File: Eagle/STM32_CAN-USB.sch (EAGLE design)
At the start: 42 parts, among them IC1 STM32F105RBT, IC2 TJA1055T, IC4 LM1117IMPX-3.3, Q1 16MHz, X1 MINI-USB

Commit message: Revert sch & brd
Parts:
- removed MC34063: MC34063, STM32_CAN-USB:MC34063
- removed R11: 3K, rcl:R-EU_R0805
- added C15: 10uF, rcl:CPOL-US153CLV-0605
- added C19, C22: 1nF, rcl:C-EUC0805
- added C20, C23: 0.1, rcl:C-EUC0805
- added C21, C24: 4.7uF, rcl:C-EUC0805
- added D1: SS26, STM32_CAN-USB:SCHOTTKY-DIODESMD
- added D2: SK36A, STM32_CAN-USB:SK36A
- added DR2: CDRH3D16NP 6.8uH, STM32_CAN-USB:CDRH3D16NP
- added F1: EST-157000 2A, STM32_CAN-USB:FUSE
- added IC3: BD9G101G, STM32_CAN-USB:BD9G101G
- C11: value 10uF/16v -> 100uF/16v; device rcl:CPOL-EUSMCA -> rcl:CPOL-US153CLV-0605
- C12: value 220uF/35V -> 0.015uF; device rcl:CPOL-EU153CLV-0810 -> rcl:C-EUC0805
- C13: value 220pF -> 0.1
- C14: value 220uF/35V -> 4.7uF/50v; device rcl:CPOL-EU153CLV-0810 -> rcl:CPOL-US153CLV-0605
- C16: value 220uF/16 -> 10uF
- D3: value SS14 -> SM6T18CA; device STM32_CAN-USB:SS14 -> STM32_CAN-USB:SM6T18CA
- DR1: value 220uH -> CDRH127 100u
- R7: value 0.33 -> 680
- R8: value 1K -> 3.9K
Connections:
- net TJA_EN renamed N$14
- net TJA_ERR renamed N$15
- net TJA_RXD renamed N$4
- net TJA_STB renamed N$6
- net TJA_TXD renamed N$5
- new net N$17: C22.1, C23.1, C24.1, D2.A, D3.2, DR1.2
- net +12V: now also F1.1; no longer C12.+, MC34063.VIN, R7.1
- net +5V: now also C13.2, C15.+, DR2.2, R8.1; no longer C14.+, DR1.1, R11.1
- net BAT: now also C14.+, D2.C, IC3.VCC
- net EN: now also IC3.EN
- net GND: now also C15.-, C19.2, C20.2, C21.2, C22.2, C23.2, C24.2, D1.A, D3.1, IC3.GND, R7.1; no longer C12.-, C13.2, D3.A, MC34063.GND, R8.2
- net N$12: now also C12.2, D1.C, DR2.1, IC3.LX; no longer MC34063.CMPR, R11.2, R8.1
- net N$13: now also C13.1, IC3.FB, R7.2, R8.2; no longer D3.C, DR1.2, MC34063.SWE
- net N$18: now also C19.1, C20.1, C21.1, DR1.1, F1.2; no longer C13.1, MC34063.CT
- net N$9: now also C12.1, IC3.BST; no longer MC34063.DRVC, MC34063.IPK, MC34063.SWC, R7.2
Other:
- moved on the sheet: C11, C13, C14, C16, C17, C18, DR1, IC4, JP1, R7, R8

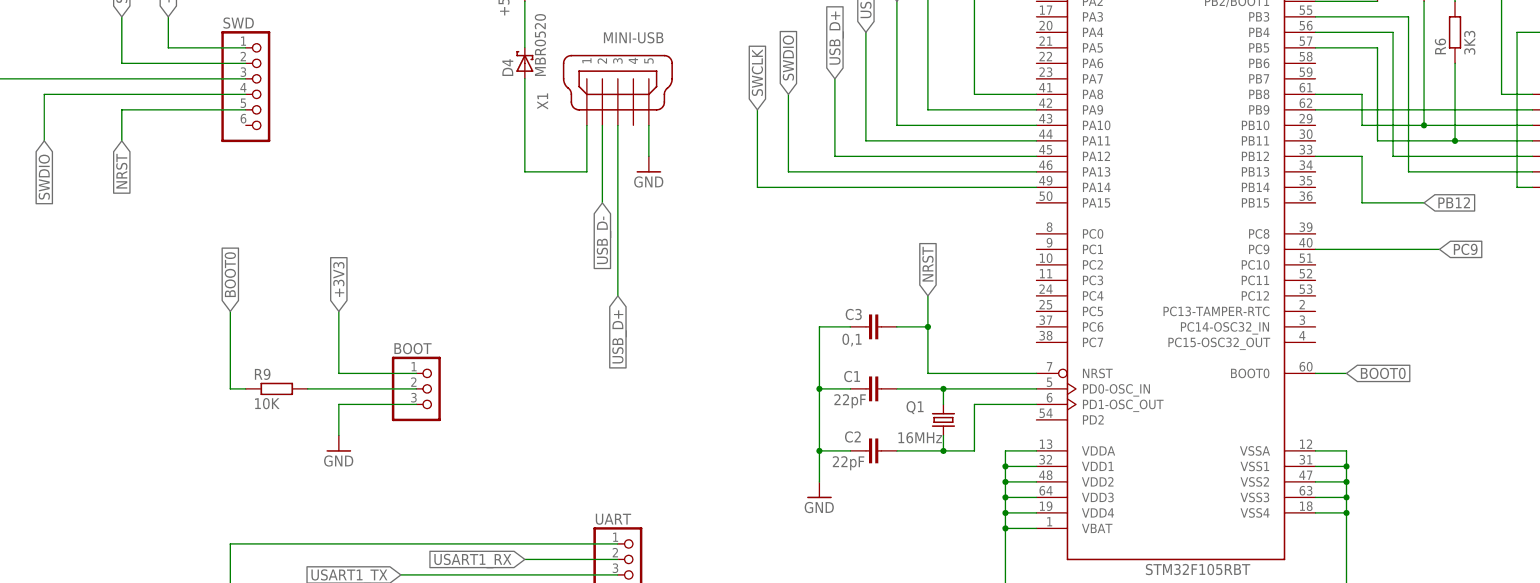
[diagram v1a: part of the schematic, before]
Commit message: delete boot, edit SWD
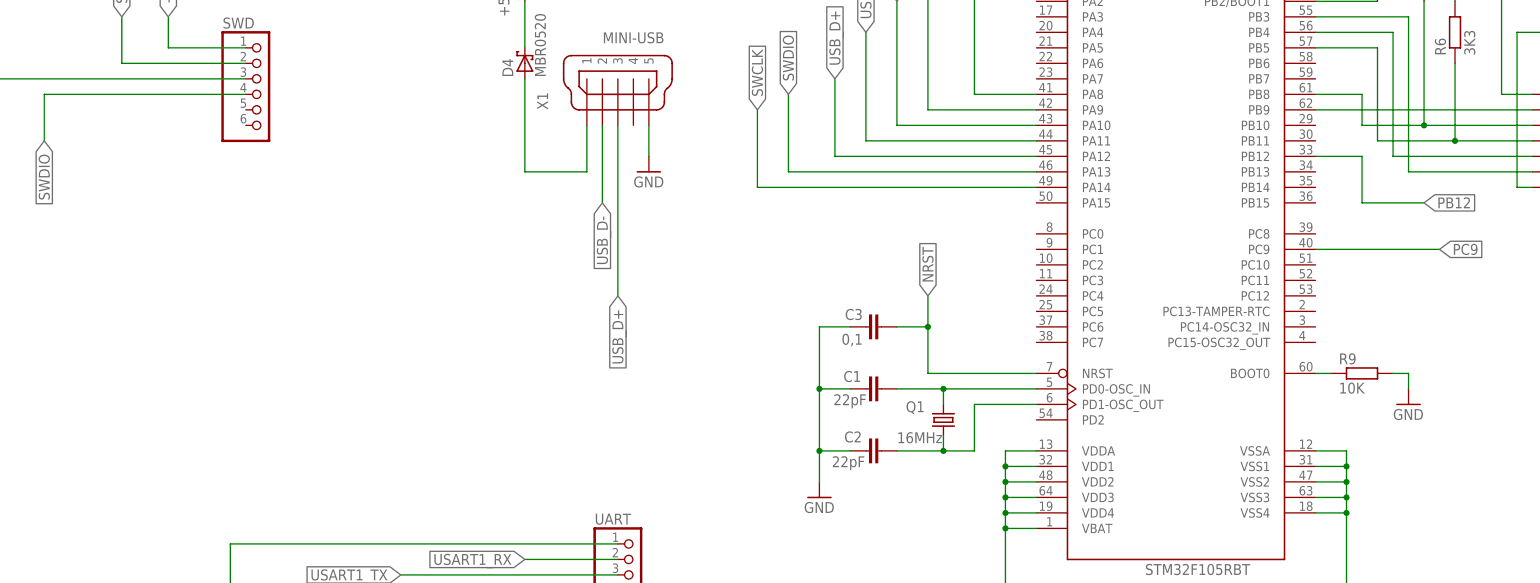
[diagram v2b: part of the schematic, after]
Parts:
- removed BOOT: (no value), pinhead:PINHD-1X3
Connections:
- net BOOT0 renamed N$3
- removed net N$3 (its old number): BOOT.2, R9.2
- net +3V3: no longer BOOT.1
- net GND: now also R9.2; no longer BOOT.3
- net NRST: no longer SWD.5
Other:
- moved on the sheet: R9
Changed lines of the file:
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@@
 <grid distance="0.1" unitdist="inch" unit="inch" style="lines" multiple="1" display="no" altdistance="0.01" altunitdist="inch" altunit="inch"/>
 <layers>
-<layer number="1" name="Top" color="4" fill="1" visible="no" active="no"/>
-<layer number="16" name="Bottom" color="1" fill="1" visible="no" active="no"/>
-<layer number="17" name="Pads" color="2" fill="1" visible="no" active="no"/>
-<layer number="18" name="Vias" color="2" fill="1" visible="no" active="no"/>
-<layer number="19" name="Unrouted" color="6" fill="1" visible="no" active="no"/>
-<layer number="20" name="Dimension" color="15" fill="1" visible="no" active="no"/>
-<layer number="21" name="tPlace" color="7" fill="1" visible="no" active="no"/>
-<layer number="22" name="bPlace" color="7" fill="1" visible="no" active="no"/>
-<layer number="23" name="tOrigins" color="15" fill="1" visible="no" active="no"/>
-<layer number="24" name="bOrigins" color="15" fill="1" visible="no" active="no"/>
-<layer number="25" name="tNames" color="7" fill="1" visible="no" active="no"/>
-<layer number="26" name="bNames" color="7" fill="1" visible="no" active="no"/>
-<layer number="27" name="tValues" color="7" fill="1" visible="no" active="no"/>
-<layer number="28" name="bValues" color="7" fill="1" visible="no" active="no"/>
+<layer number="1" name="Top" color="4" fill="1" visible="yes" active="no"/>
+<layer number="16" name="Bottom" color="1" fill="1" visible="yes" active="no"/>
+<layer number="17" name="Pads" color="2" fill="1" visible="yes" active="no"/>
+<layer number="18" name="Vias" color="2" fill="1" visible="yes" active="no"/>
+<layer number="19" name="Unrouted" color="6" fill="1" visible="yes" active="no"/>
+<layer number="20" name="Dimension" color="15" fill="1" visible="yes" active="no"/>
+<layer number="21" name="tPlace" color="7" fill="1" visible="yes" active="no"/>
+<layer number="22" name="bPlace" color="7" fill="1" visible="yes" active="no"/>
+<layer number="23" name="tOrigins" color="15" fill="1" visible="yes" active="no"/>
+<layer number="24" name="bOrigins" color="15" fill="1" visible="yes" active="no"/>
+<layer number="25" name="tNames" color="7" fill="1" visible="yes" active="no"/>
+<layer number="26" name="bNames" color="7" fill="1" visible="yes" active="no"/>
+<layer number="27" name="tValues" color="7" fill="1" visible="yes" active="no"/>
+<layer number="28" name="bValues" color="7" fill="1" visible="yes" active="no"/>
 <layer number="29" name="tStop" color="7" fill="3" visible="no" active="no"/>
 <layer number="30" name="bStop" color="7" fill="6" visible="no" active="no"/>
@@
 <layer number="35" name="tGlue" color="7" fill="4" visible="no" active="no"/>
 <layer number="36" name="bGlue" color="7" fill="5" visible="no" active="no"/>
-<layer number="37" name="tTest" color="7" fill="1" visible="no" active="no"/>
-<layer number="38" name="bTest" color="7" fill="1" visible="no" active="no"/>
+<layer number="37" name="tTest" color="7" fill="1" visible="yes" active="no"/>
+<layer number="38" name="bTest" color="7" fill="1" visible="yes" active="no"/>
 <layer number="39" name="tKeepout" color="4" fill="11" visible="no" active="no"/>
 <layer number="40" name="bKeepout" color="1" fill="11" visible="no" active="no"/>
@@
 <layer number="44" name="Drills" color="7" fill="1" visible="no" active="no"/>
 <layer number="45" name="Holes" color="7" fill="1" visible="no" active="no"/>
-<layer number="46" name="Milling" color="3" fill="1" visible="no" active="no"/>
-<layer number="47" name="Measures" color="7" fill="1" visible="no" active="no"/>
-<layer number="48" name="Document" color="7" fill="1" visible="no" active="no"/>
-<layer number="49" name="Reference" color="7" fill="1" visible="no" active="no"/>
-<layer number="51" name="tDocu" color="7" fill="1" visible="no" active="no"/>
-<layer number="52" name="bDocu" color="7" fill="1" visible="no" active="no"/>
+<layer number="46" name="Milling" color="3" fill="1" visible="yes" active="no"/>
+<layer number="47" name="Measures" color="7" fill="1" visible="yes" active="no"/>
+<layer number="48" name="Document" color="7" fill="1" visible="yes" active="no"/>
+<layer number="49" name="Reference" color="7" fill="1" visible="yes" active="no"/>
+<layer number="51" name="tDocu" color="7" fill="1" visible="yes" active="no"/>
+<layer number="52" name="bDocu" color="7" fill="1" visible="yes" active="no"/>
 <layer number="90" name="Modules" color="5" fill="1" visible="yes" active="yes"/>
 <layer number="91" name="Nets" color="2" fill="1" visible="yes" active="yes"/>
@@
 <part name="SWD" library="pinhead" deviceset="PINHD-1X6" device=""/>
 <part name="GND14" library="supply1" deviceset="GND" device=""/>
-<part name="BOOT" library="pinhead" deviceset="PINHD-1X3" device=""/>
 <part name="R9" library="rcl" deviceset="R-EU_" device="R0805" value="10K"/>
 <part name="GND15" library="supply1" deviceset="GND" device=""/>
@@
 <instance part="SWD" gate="A" x="-83.82" y="71.12"/>
 <instance part="GND14" gate="1" x="-132.08" y="55.88"/>
-<instance part="BOOT" gate="A" x="-55.88" y="22.86"/>
-<instance part="R9" gate="G$1" x="-81.28" y="22.86"/>
+<instance part="R9" gate="G$1" x="96.52" y="25.4"/>
 <instance part="GND15" gate="1" x="93.98" y="99.06"/>
 <instance part="R10" gate="G$1" x="99.06" y="91.44" rot="R90"/>
-<instance part="GND16" gate="1" x="-71.12" y="12.7"/>
+<instance part="GND16" gate="1" x="104.14" y="20.32"/>
 <instance part="UART" gate="A" x="-22.86" y="-5.08"/>
 <instance part="GND17" gate="1" x="-88.9" y="-15.24"/>
@@
 </segment>
 <segment>
-<pinref part="GND16" gate="1" pin="GND"/>
-<pinref part="BOOT" gate="A" pin="3"/>
-<wire x1="-71.12" y1="15.24" x2="-71.12" y2="20.32" width="0.1524" layer="91"/>
-<wire x1="-71.12" y1="20.32" x2="-58.42" y2="20.32" width="0.1524" layer="91"/>
-</segment>
-<segment>
 <pinref part="UART" gate="A" pin="1"/>
 <pinref part="GND17" gate="1" pin="GND"/>
 <wire x1="-25.4" y1="-2.54" x2="-88.9" y2="-2.54" width="0.1524" layer="91"/>
 <wire x1="-88.9" y1="-2.54" x2="-88.9" y2="-12.7" width="0.1524" layer="91"/>
+</segment>
+<segment>
+<pinref part="R9" gate="G$1" pin="2"/>
+<pinref part="GND16" gate="1" pin="GND"/>
+<wire x1="101.6" y1="25.4" x2="104.14" y2="25.4" width="0.1524" layer="91"/>
+<wire x1="104.14" y1="25.4" x2="104.14" y2="22.86" width="0.1524" layer="91"/>
 </segment>
 </net>
@@
 <label x="-99.06" y="83.82" size="1.778" layer="95" rot="R90" xref="yes"/>
 </segment>
-<segment>
-<pinref part="BOOT" gate="A" pin="1"/>
-<wire x1="-58.42" y1="25.4" x2="-71.12" y2="25.4" width="0.1524" layer="91"/>
-<wire x1="-71.12" y1="25.4" x2="-71.12" y2="35.56" width="0.1524" layer="91"/>
-<label x="-71.12" y="35.56" size="1.778" layer="95" rot="R90" xref="yes"/>
-</segment>
 </net>
 <net name="N$4" class="0">
@@
 <net name="NRST" class="0">
 <segment>
-<pinref part="SWD" gate="A" pin="5"/>
-<wire x1="-86.36" y1="68.58" x2="-106.68" y2="68.58" width="0.1524" layer="91"/>
-<wire x1="-106.68" y1="68.58" x2="-106.68" y2="63.5" width="0.1524" layer="91"/>
-<label x="-106.68" y="63.5" size="1.778" layer="95" rot="R270" xref="yes"/>
-</segment>
-<segment>
 <pinref part="C3" gate="G$1" pin="2"/>
 <wire x1="20.32" y1="33.02" x2="25.4" y2="33.02" width="0.1524" layer="91"/>
@@
 </segment>
 </net>
-<net name="N$3" class="0">
-<segment>
-<pinref part="R9" gate="G$1" pin="2"/>
-<pinref part="BOOT" gate="A" pin="2"/>
-<wire x1="-76.2" y1="22.86" x2="-58.42" y2="22.86" width="0.1524" layer="91"/>
-</segment>
-</net>
 <net name="N$16" class="0">
 <segment>
@@
 <pinref part="R10" gate="G$1" pin="1"/>
 <wire x1="88.9" y1="86.36" x2="99.06" y2="86.36" width="0.1524" layer="91"/>
-</segment>
-</net>
-<net name="BOOT0" class="0">
-<segment>
-<pinref part="R9" gate="G$1" pin="1"/>
-<wire x1="-86.36" y1="22.86" x2="-88.9" y2="22.86" width="0.1524" layer="91"/>
-<wire x1="-88.9" y1="22.86" x2="-88.9" y2="35.56" width="0.1524" layer="91"/>
-<label x="-88.9" y="35.56" size="1.778" layer="95" rot="R90" xref="yes"/>
-</segment>
-<segment>
-<pinref part="IC1" gate="MCU" pin="BOOT0"/>
-<wire x1="88.9" y1="25.4" x2="93.98" y2="25.4" width="0.1524" layer="91"/>
-<label x="93.98" y="25.4" size="1.778" layer="95" xref="yes"/>
 </segment>
 </net>
@@
 </segment>
 </net>
+<net name="N$3" class="0">
+<segment>
+<pinref part="IC1" gate="MCU" pin="BOOT0"/>
+<pinref part="R9" gate="G$1" pin="1"/>
+<wire x1="88.9" y1="25.4" x2="91.44" y2="25.4" width="0.1524" layer="91"/>
+</segment>
+</net>

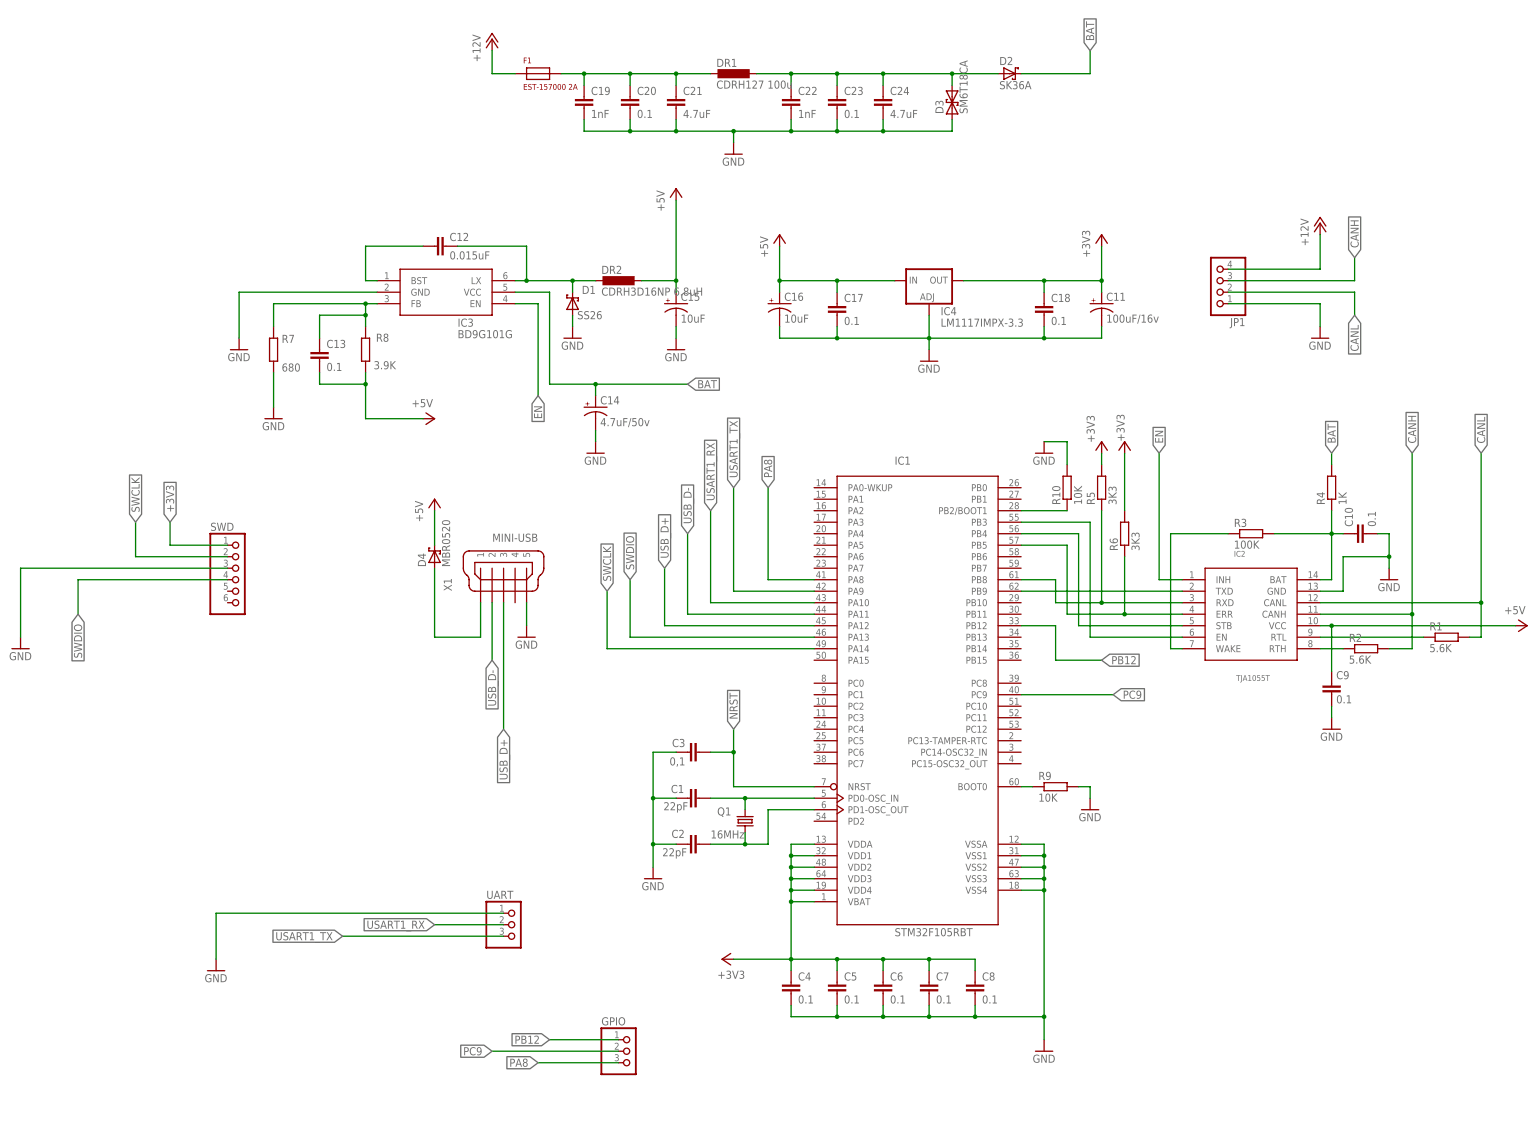
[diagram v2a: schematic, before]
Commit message: Labels, pin headers optimization
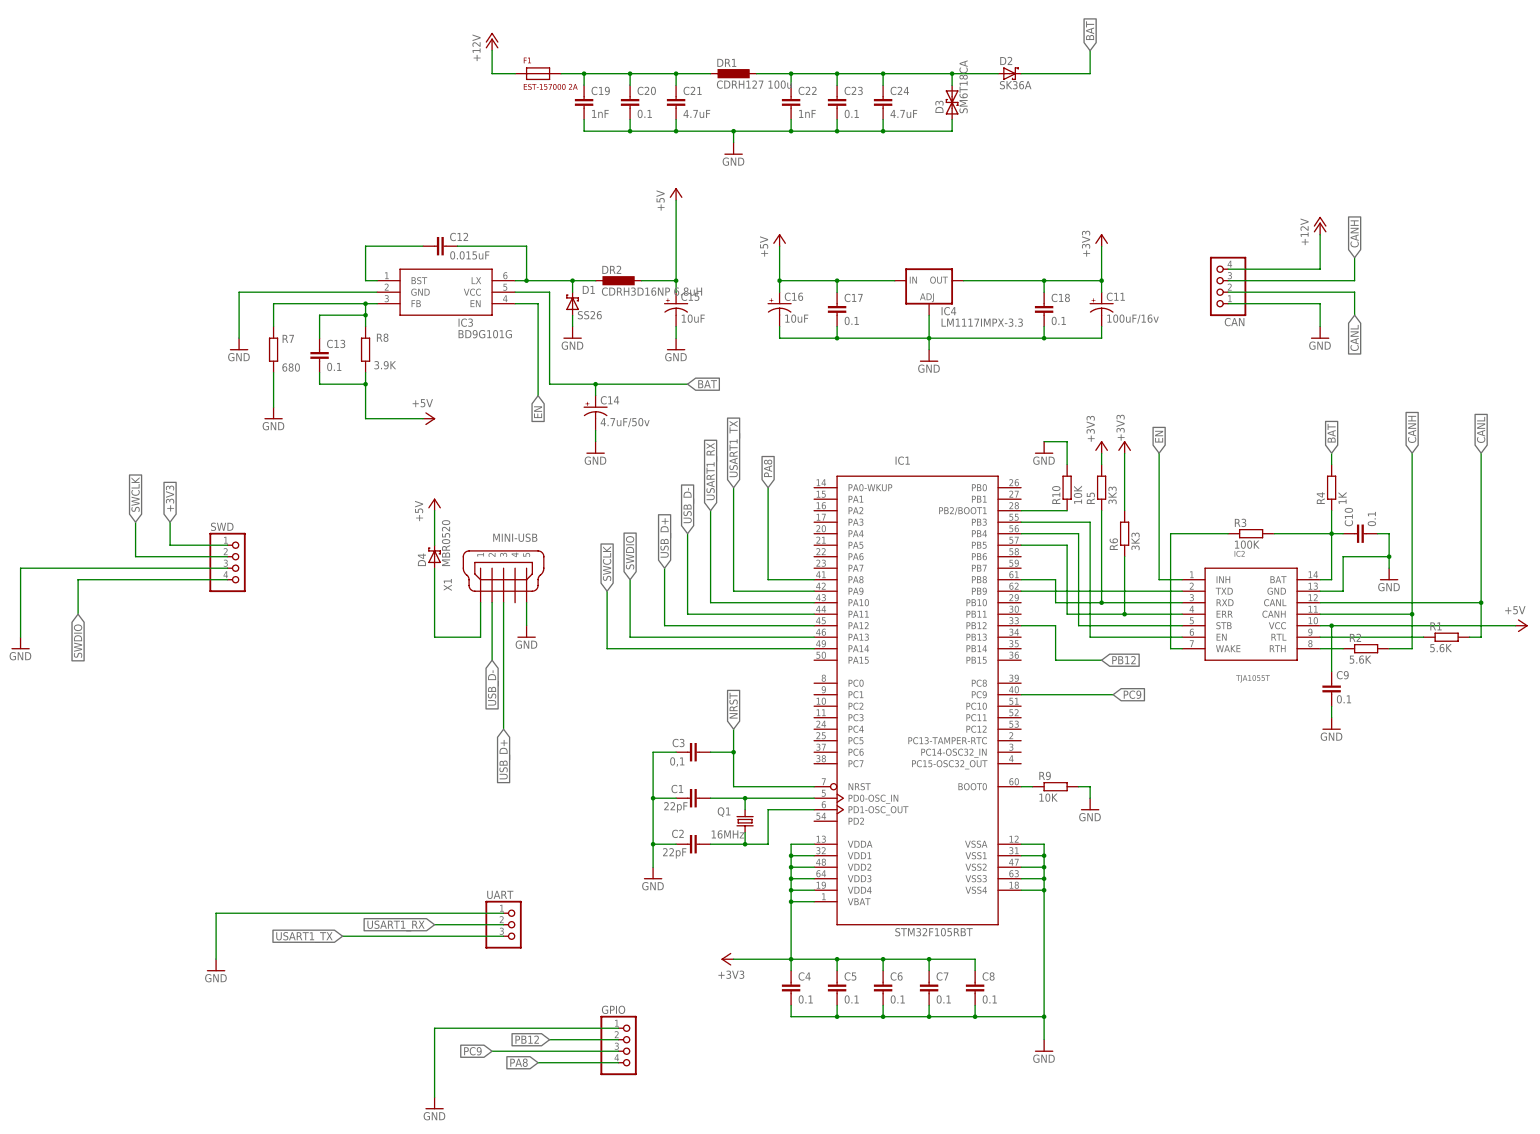
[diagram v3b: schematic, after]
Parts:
- GPIO: device pinhead:PINHD-1X3 -> pinhead:PINHD-1X4
- SWD: device pinhead:PINHD-1X6 -> pinhead:PINHD-1X4
- renumbered JP1 to CAN
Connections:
- net GND: now also GPIO.1
- net PA8: now also GPIO.4; no longer GPIO.3
- net PB12: now also GPIO.2; no longer GPIO.1
- net PC9: now also GPIO.3; no longer GPIO.2
